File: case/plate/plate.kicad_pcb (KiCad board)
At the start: 2 copper layers, 121.2 x 102.2 mm, 0 parts

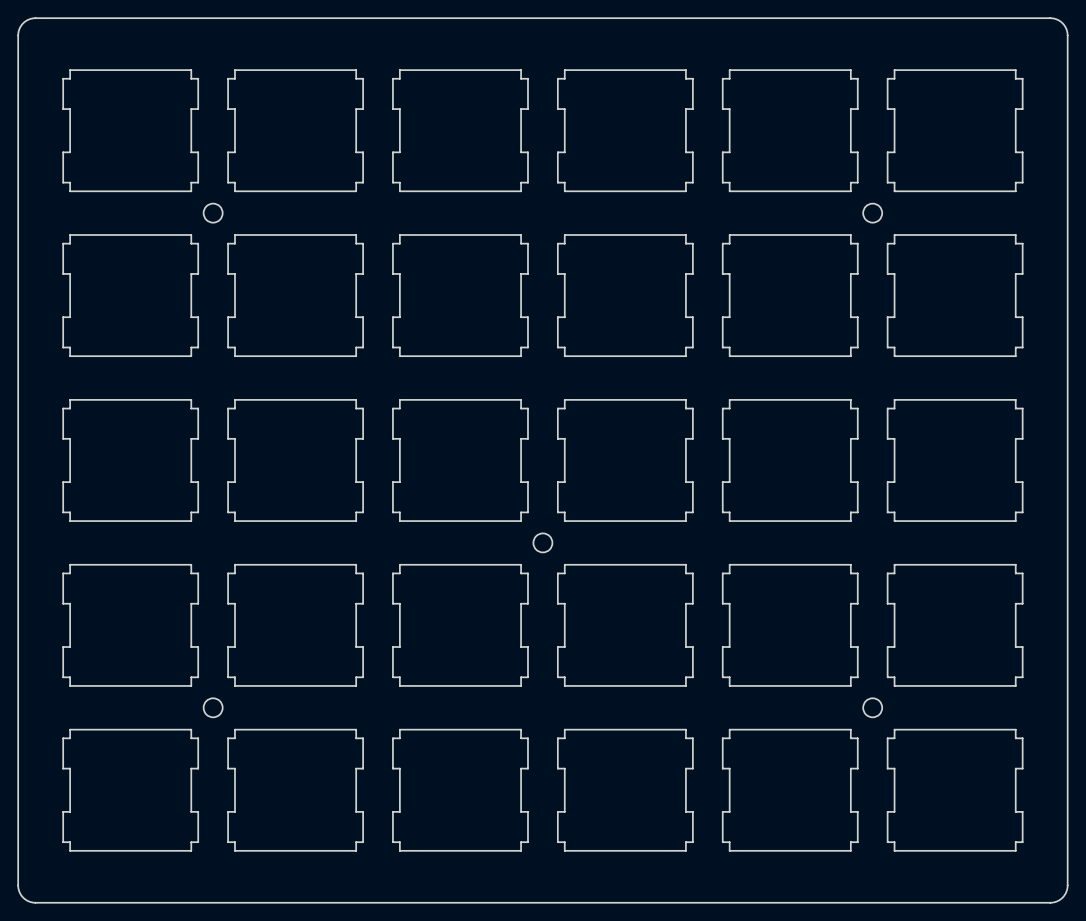
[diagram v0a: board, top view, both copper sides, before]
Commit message: Circles to holes
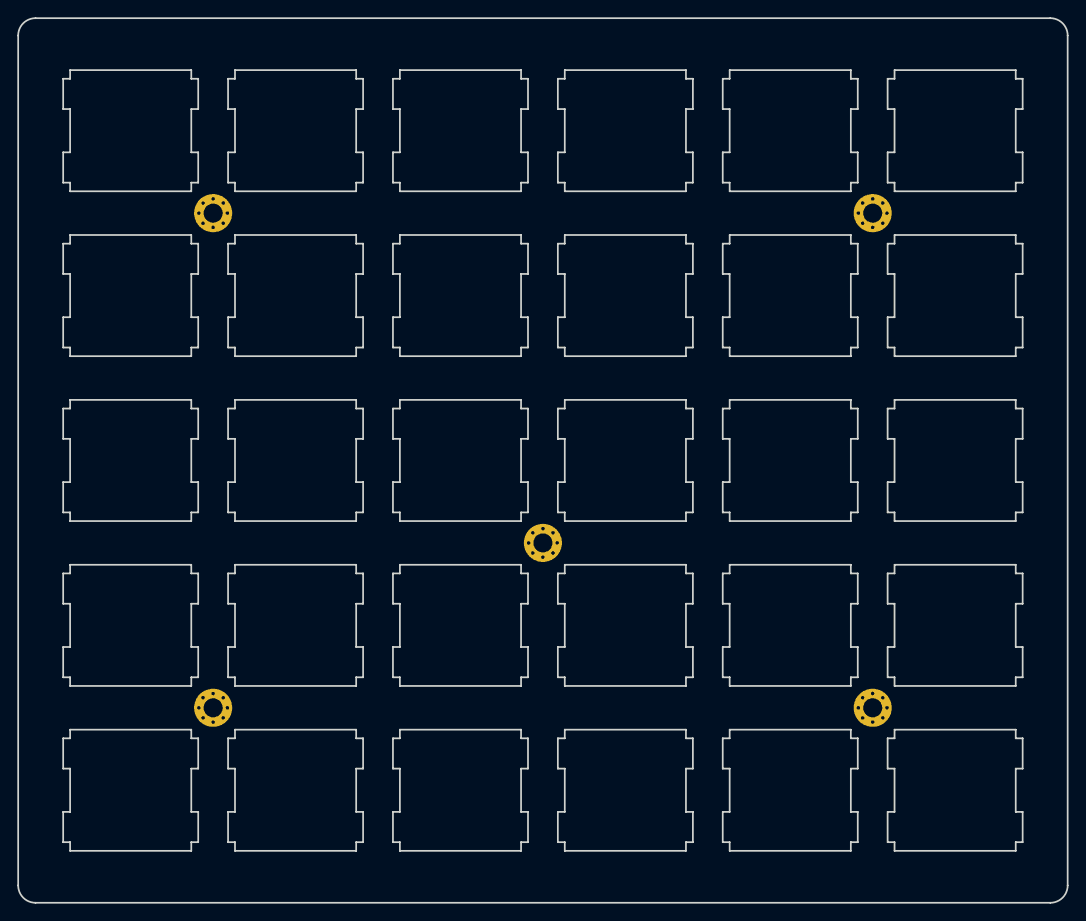
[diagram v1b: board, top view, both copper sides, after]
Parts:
- added REF**: MountingHole_2.2mm_M2_Pad_Via, MountingHole_2.2mm_M2_Pad_Via, F.Cu at (109.5, 116.7)
- added REF**: MountingHole_2.2mm_M2_Pad_Via, MountingHole_2.2mm_M2_Pad_Via, F.Cu at (185.7, 116.7)
- added REF**: MountingHole_2.2mm_M2_Pad_Via, MountingHole_2.2mm_M2_Pad_Via, F.Cu at (147.6, 97.6)
- added REF**: MountingHole_2.2mm_M2_Pad_Via, MountingHole_2.2mm_M2_Pad_Via, F.Cu at (109.5, 59.5)
- added REF**: MountingHole_2.2mm_M2_Pad_Via, MountingHole_2.2mm_M2_Pad_Via, F.Cu at (185.7, 59.5)
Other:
- outline, holes or cut-outs redrawn
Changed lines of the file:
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@@
     (tracks 0)
     (zones 0)
-    (modules 0)
+    (modules 5)
     (nets 1)
   )
@@
     (uvia_drill 0.1)
   )
+  (module MountingHole_2.2mm_M2_Pad_Via (layer F.Cu)
+    (at 109.525 116.675)
+    (descr "Mounting Hole 2.2mm, M2")
+    (tags "mounting hole 2.2mm m2")
+    (attr virtual)
+    (fp_text reference REF** (at 0 -3.2) (layer F.SilkS) hide
+      (effects (font (size 1 1) (thickness 0.15)))
+    )
+    (fp_text value MountingHole_2.2mm_M2_Pad_Via (at 0 3.2) (layer F.Fab)
+      (effects (font (size 1 1) (thickness 0.15)))
+    )
+    (fp_circle (center 0 0) (end 2.45 0) (layer F.CrtYd) (width 0.05))
+    (fp_circle (center 0 0) (end 2.2 0) (layer Cmts.User) (width 0.15))
+    (fp_text user %R (at 0.3 0) (layer F.Fab)
+      (effects (font (size 1 1) (thickness 0.15)))
+    )
+    (pad 1 thru_hole circle (at 1.166726 -1.166726) (size 0.7 0.7) (drill 0.4) (layers *.Cu *.Mask))
+    (pad 1 thru_hole circle (at 0 -1.65) (size 0.7 0.7) (drill 0.4) (layers *.Cu *.Mask))
+    (pad 1 thru_hole circle (at -1.166726 -1.166726) (size 0.7 0.7) (drill 0.4) (layers *.Cu *.Mask))
+    (pad 1 thru_hole circle (at -1.65 0) (size 0.7 0.7) (drill 0.4) (layers *.Cu *.Mask))
+    (pad 1 thru_hole circle (at -1.166726 1.166726) (size 0.7 0.7) (drill 0.4) (layers *.Cu *.Mask))
+    (pad 1 thru_hole circle (at 0 1.65) (size 0.7 0.7) (drill 0.4) (layers *.Cu *.Mask))
+    (pad 1 thru_hole circle (at 1.166726 1.166726) (size 0.7 0.7) (drill 0.4) (layers *.Cu *.Mask))
+    (pad 1 thru_hole circle (at 1.65 0) (size 0.7 0.7) (drill 0.4) (layers *.Cu *.Mask))
+    (pad 1 thru_hole circle (at 0 0) (size 4.4 4.4) (drill 2.2) (layers *.Cu *.Mask))
+  )
+  (module MountingHole_2.2mm_M2_Pad_Via (layer F.Cu)
+    (at 185.725 116.675)
+    (descr "Mounting Hole 2.2mm, M2")
+    (tags "mounting hole 2.2mm m2")
+    (attr virtual)
+    (fp_text reference REF** (at 0 -3.2) (layer F.SilkS) hide
+      (effects (font (size 1 1) (thickness 0.15)))
+    )
+    (fp_text value MountingHole_2.2mm_M2_Pad_Via (at 0 3.2) (layer F.Fab)
+      (effects (font (size 1 1) (thickness 0.15)))
+    )
+    (fp_circle (center 0 0) (end 2.45 0) (layer F.CrtYd) (width 0.05))
+    (fp_circle (center 0 0) (end 2.2 0) (layer Cmts.User) (width 0.15))
+    (fp_text user %R (at 0.3 0) (layer F.Fab)
+      (effects (font (size 1 1) (thickness 0.15)))
+    )
+    (pad 1 thru_hole circle (at 1.166726 -1.166726) (size 0.7 0.7) (drill 0.4) (layers *.Cu *.Mask))
+    (pad 1 thru_hole circle (at 0 -1.65) (size 0.7 0.7) (drill 0.4) (layers *.Cu *.Mask))
+    (pad 1 thru_hole circle (at -1.166726 -1.166726) (size 0.7 0.7) (drill 0.4) (layers *.Cu *.Mask))
+    (pad 1 thru_hole circle (at -1.65 0) (size 0.7 0.7) (drill 0.4) (layers *.Cu *.Mask))
+    (pad 1 thru_hole circle (at -1.166726 1.166726) (size 0.7 0.7) (drill 0.4) (layers *.Cu *.Mask))
+    (pad 1 thru_hole circle (at 0 1.65) (size 0.7 0.7) (drill 0.4) (layers *.Cu *.Mask))
+    (pad 1 thru_hole circle (at 1.166726 1.166726) (size 0.7 0.7) (drill 0.4) (layers *.Cu *.Mask))
+    (pad 1 thru_hole circle (at 1.65 0) (size 0.7 0.7) (drill 0.4) (layers *.Cu *.Mask))
+    (pad 1 thru_hole circle (at 0 0) (size 4.4 4.4) (drill 2.2) (layers *.Cu *.Mask))
+  )
+  (module MountingHole_2.2mm_M2_Pad_Via (layer F.Cu)
+    (at 147.625 97.625)
+    (descr "Mounting Hole 2.2mm, M2")
+    (tags "mounting hole 2.2mm m2")
+    (attr virtual)
+    (fp_text reference REF** (at 0 -3.2) (layer F.SilkS) hide
+      (effects (font (size 1 1) (thickness 0.15)))
+    )
+    (fp_text value MountingHole_2.2mm_M2_Pad_Via (at 0 3.2) (layer F.Fab)
+      (effects (font (size 1 1) (thickness 0.15)))
+    )
+    (fp_circle (center 0 0) (end 2.45 0) (layer F.CrtYd) (width 0.05))
+    (fp_circle (center 0 0) (end 2.2 0) (layer Cmts.User) (width 0.15))
+    (fp_text user %R (at 0.3 0) (layer F.Fab)
+      (effects (font (size 1 1) (thickness 0.15)))
+    )
+    (pad 1 thru_hole circle (at 1.166726 -1.166726) (size 0.7 0.7) (drill 0.4) (layers *.Cu *.Mask))
+    (pad 1 thru_hole circle (at 0 -1.65) (size 0.7 0.7) (drill 0.4) (layers *.Cu *.Mask))
+    (pad 1 thru_hole circle (at -1.166726 -1.166726) (size 0.7 0.7) (drill 0.4) (layers *.Cu *.Mask))
+    (pad 1 thru_hole circle (at -1.65 0) (size 0.7 0.7) (drill 0.4) (layers *.Cu *.Mask))
+    (pad 1 thru_hole circle (at -1.166726 1.166726) (size 0.7 0.7) (drill 0.4) (layers *.Cu *.Mask))
+    (pad 1 thru_hole circle (at 0 1.65) (size 0.7 0.7) (drill 0.4) (layers *.Cu *.Mask))
+    (pad 1 thru_hole circle (at 1.166726 1.166726) (size 0.7 0.7) (drill 0.4) (layers *.Cu *.Mask))
+    (pad 1 thru_hole circle (at 1.65 0) (size 0.7 0.7) (drill 0.4) (layers *.Cu *.Mask))
+    (pad 1 thru_hole circle (at 0 0) (size 4.4 4.4) (drill 2.2) (layers *.Cu *.Mask))
+  )
+  (module MountingHole_2.2mm_M2_Pad_Via (layer F.Cu)
+    (at 109.525 59.525)
+    (descr "Mounting Hole 2.2mm, M2")
+    (tags "mounting hole 2.2mm m2")
+    (attr virtual)
+    (fp_text reference REF** (at 0 -3.2) (layer F.SilkS) hide
+      (effects (font (size 1 1) (thickness 0.15)))
+    )
+    (fp_text value MountingHole_2.2mm_M2_Pad_Via (at 0 3.2) (layer F.Fab)
+      (effects (font (size 1 1) (thickness 0.15)))
+    )
+    (fp_circle (center 0 0) (end 2.45 0) (layer F.CrtYd) (width 0.05))
+    (fp_circle (center 0 0) (end 2.2 0) (layer Cmts.User) (width 0.15))
+    (fp_text user %R (at 0.3 0) (layer F.Fab)
+      (effects (font (size 1 1) (thickness 0.15)))
+    )
+    (pad 1 thru_hole circle (at 1.166726 -1.166726) (size 0.7 0.7) (drill 0.4) (layers *.Cu *.Mask))
+    (pad 1 thru_hole circle (at 0 -1.65) (size 0.7 0.7) (drill 0.4) (layers *.Cu *.Mask))
+    (pad 1 thru_hole circle (at -1.166726 -1.166726) (size 0.7 0.7) (drill 0.4) (layers *.Cu *.Mask))
+    (pad 1 thru_hole circle (at -1.65 0) (size 0.7 0.7) (drill 0.4) (layers *.Cu *.Mask))
+    (pad 1 thru_hole circle (at -1.166726 1.166726) (size 0.7 0.7) (drill 0.4) (layers *.Cu *.Mask))
+    (pad 1 thru_hole circle (at 0 1.65) (size 0.7 0.7) (drill 0.4) (layers *.Cu *.Mask))
+    (pad 1 thru_hole circle (at 1.166726 1.166726) (size 0.7 0.7) (drill 0.4) (layers *.Cu *.Mask))
+    (pad 1 thru_hole circle (at 1.65 0) (size 0.7 0.7) (drill 0.4) (layers *.Cu *.Mask))
+    (pad 1 thru_hole circle (at 0 0) (size 4.4 4.4) (drill 2.2) (layers *.Cu *.Mask))
+  )
+  (module MountingHole_2.2mm_M2_Pad_Via (layer F.Cu)
+    (at 185.725 59.525)
+    (descr "Mounting Hole 2.2mm, M2")
+    (tags "mounting hole 2.2mm m2")
+    (attr virtual)
+    (fp_text reference REF** (at 0 -3.2) (layer F.SilkS) hide
+      (effects (font (size 1 1) (thickness 0.15)))
+    )
+    (fp_text value MountingHole_2.2mm_M2_Pad_Via (at 0 3.2) (layer F.Fab)
+      (effects (font (size 1 1) (thickness 0.15)))
+    )
+    (fp_circle (center 0 0) (end 2.45 0) (layer F.CrtYd) (width 0.05))
+    (fp_circle (center 0 0) (end 2.2 0) (layer Cmts.User) (width 0.15))
+    (fp_text user %R (at 0.3 0) (layer F.Fab)
+      (effects (font (size 1 1) (thickness 0.15)))
+    )
+    (pad 1 thru_hole circle (at 1.166726 -1.166726) (size 0.7 0.7) (drill 0.4) (layers *.Cu *.Mask))
+    (pad 1 thru_hole circle (at 0 -1.65) (size 0.7 0.7) (drill 0.4) (layers *.Cu *.Mask))
+    (pad 1 thru_hole circle (at -1.166726 -1.166726) (size 0.7 0.7) (drill 0.4) (layers *.Cu *.Mask))
+    (pad 1 thru_hole circle (at -1.65 0) (size 0.7 0.7) (drill 0.4) (layers *.Cu *.Mask))
+    (pad 1 thru_hole circle (at -1.166726 1.166726) (size 0.7 0.7) (drill 0.4) (layers *.Cu *.Mask))
+    (pad 1 thru_hole circle (at 0 1.65) (size 0.7 0.7) (drill 0.4) (layers *.Cu *.Mask))
+    (pad 1 thru_hole circle (at 1.166726 1.166726) (size 0.7 0.7) (drill 0.4) (layers *.Cu *.Mask))
+    (pad 1 thru_hole circle (at 1.65 0) (size 0.7 0.7) (drill 0.4) (layers *.Cu *.Mask))
+    (pad 1 thru_hole circle (at 0 0) (size 4.4 4.4) (drill 2.2) (layers *.Cu *.Mask))
+  )
   (gr_line (start 203.05 56) (end 202.25 56) (layer Edge.Cuts) (width 0.2))
   (gr_line (start 203.05 52.5) (end 203.05 56) (layer Edge.Cuts) (width 0.2))
@@
   (gr_line (start 187.45 47.5) (end 187.45 44) (layer Edge.Cuts) (width 0.2))
   (gr_line (start 187.45 44) (end 188.25 44) (layer Edge.Cuts) (width 0.2))
-  (gr_circle (center 185.725 59.525) (end 186.825 59.525) (layer Edge.Cuts) (width 0.2))
-  (gr_circle (center 109.525 59.525) (end 110.625 59.525) (layer Edge.Cuts) (width 0.2))
+  (gr_circle (center 185.725 59.525) (end 186.825 59.525) (layer Eco1.User) (width 0.2))
+  (gr_circle (center 109.525 59.525) (end 110.625 59.525) (layer Eco1.User) (width 0.2))
   (gr_line (start 126.85 56) (end 126.05 56) (layer Edge.Cuts) (width 0.2))
   (gr_line (start 126.85 52.5) (end 126.85 56) (layer Edge.Cuts) (width 0.2))
@@
   (gr_line (start 187.45 66.55) (end 187.45 63.05) (layer Edge.Cuts) (width 0.2))
   (gr_line (start 187.45 63.05) (end 188.25 63.05) (layer Edge.Cuts) (width 0.2))
-  (gr_circle (center 147.625 97.625) (end 148.725 97.625) (layer Edge.Cuts) (width 0.2))
+  (gr_circle (center 147.625 97.625) (end 148.725 97.625) (layer Eco1.User) (width 0.2))
   (gr_line (start 126.85 94.1) (end 126.05 94.1) (layer Edge.Cuts) (width 0.2))
   (gr_line (start 126.85 90.6) (end 126.85 94.1) (layer Edge.Cuts) (width 0.2))
@@
   (gr_line (start 168.399999 104.65) (end 168.4 101.15) (layer Edge.Cuts) (width 0.2))
   (gr_line (start 168.4 101.15) (end 169.2 101.15) (layer Edge.Cuts) (width 0.2))
-  (gr_circle (center 185.725 116.675) (end 186.825 116.675) (layer Edge.Cuts) (width 0.2))
-  (gr_circle (center 109.525 116.675) (end 110.625 116.675) (layer Edge.Cuts) (width 0.2))
+  (gr_circle (center 185.725 116.675) (end 186.825 116.675) (layer Eco1.User) (width 0.2))
+  (gr_circle (center 109.525 116.675) (end 110.625 116.675) (layer Eco1.User) (width 0.2))
   (gr_line (start 107.8 132.199999) (end 107 132.199999) (layer Edge.Cuts) (width 0.2))
   (gr_line (start 107.8 128.699999) (end 107.8 132.199999) (layer Edge.Cuts) (width 0.2))
